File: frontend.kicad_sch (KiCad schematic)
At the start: 48 parts, among them J10 GND_CLIP, J3 RF-SHIELD-FRAME, J4 MOUNTING_HOLE, J5 MOUNTING_HOLE, J6 MOUNTING_HOLE, J7 MOUNTING_HOLE, P4 SMA, Q1 NMOS/PMOS, U12 MXD8638C, U13 TRF37C73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

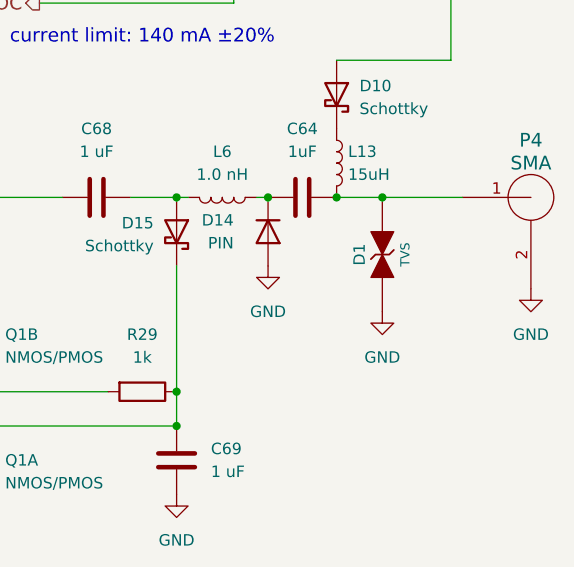
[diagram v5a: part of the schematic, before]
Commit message: Update TVS
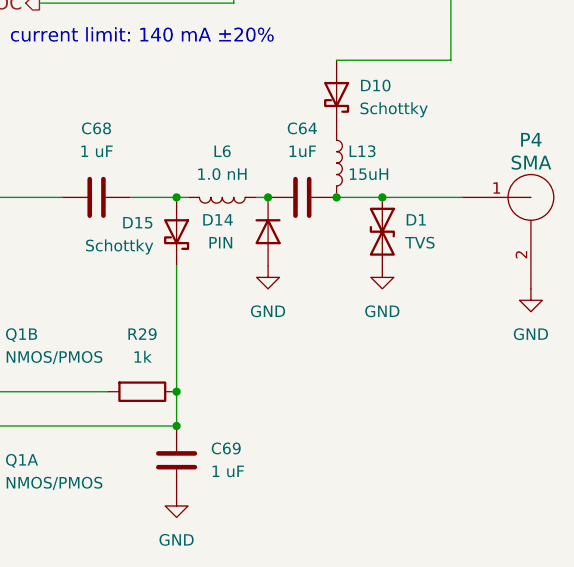
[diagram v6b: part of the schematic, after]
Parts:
- removed D1: TVS, hackrf:GSG-0402, symbol hackrf:GSG-DIODE-TVS-BI
- added D1: TVS, Diode_SMD:Nexperia_DSN0603-2_0.6x0.3mm_P0.4mm, symbol Device:D_TVS
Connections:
- net GND: now also D1.2 (A2)
- net at C64.2, L13.2, P4.1 (RF): now also D1.1 (A1)
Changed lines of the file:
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@@
 	)
 	(junction
-		(at 232.41 90.17)
-		(diameter 0)
-		(color 0 0 0 0)
-	)
-	(junction
 		(at 72.39 97.79)
 		(diameter 0)
@@
 	)
 	(junction
+		(at 232.41 90.17)
+		(diameter 0)
+		(color 0 0 0 0)
+	)
+	(junction
 		(at 127 62.23)
 		(diameter 0)
@@
 	(wire
 		(pts
+			(xy 232.41 90.17) (xy 241.3 90.17)
+		)
+		(stroke
+			(width 0)
+			(type default)
+		)
+	)
+	(wire
+		(pts
 			(xy 130.81 92.71) (xy 144.78 92.71)
 		)
@@
 	(wire
 		(pts
-			(xy 241.3 90.17) (xy 232.41 90.17)
+			(xy 227.33 90.17) (xy 232.41 90.17)
 		)
 		(stroke
@@
 	(wire
 		(pts
-			(xy 227.33 90.17) (xy 232.41 90.17)
-		)
-		(stroke
-			(width 0)
-			(type default)
-		)
-	)
-	(wire
-		(pts
 			(xy 165.1 119.38) (xy 165.1 92.71)
 		)
@@
 	)
 	(symbol
-		(lib_id "hackrf:GSG-DIODE-TVS-BI")
-		(at 232.41 96.52 90)
-		(unit 1)
-		(exclude_from_sim no)
-		(in_bom yes)
-		(on_board yes)
-		(dnp no)
-		(property "Reference" "D1"
-			(at 229.87 96.52 0)
-			(effects
-				(font
-					(size 1.27 1.27)
-				)
-			)
-		)
-		(property "Value" "TVS"
-			(at 234.95 96.52 0)
-			(effects
-				(font
-					(size 1.016 1.016)
-				)
-			)
-		)
-		(property "Footprint" "hackrf:GSG-0402"
-			(at 232.41 96.52 0)
-			(effects
-				(font
-					(size 1.524 1.524)
-				)
-				(hide yes)
-			)
-		)
-		(property "Datasheet" "~"
-			(at 232.41 96.52 0)
-			(effects
-				(font
-					(size 1.524 1.524)
-				)
-				(hide yes)
-			)
-		)
-		(property "Description" "TVS DIODE ESD .05PF 15KV 0402"
-			(at 232.41 96.52 0)
-			(effects
-				(font
-					(size 1.524 1.524)
-				)
-				(hide yes)
-			)
-		)
-		(property "Manufacturer" "TECH PUBLIC"
-			(at 232.41 96.52 0)
-			(effects
-				(font
-					(size 1.524 1.524)
-				)
-				(hide yes)
-			)
-		)
-		(property "Part Number" "LXES15AAA1-153"
-			(at 232.41 96.52 0)
-			(effects
-				(font
-					(size 1.524 1.524)
-				)
-				(hide yes)
-			)
-		)
-		(pin "1"
-		)
-		(pin "2"
-		)
-		(instances
-			(project ""
-				(path "/dba4afc6-760f-46cb-a936-032b76448f03/00000000-0000-0000-0000-0000503bb638"
-					(reference "D1")
-					(unit 1)
-				)
-			)
-		)
-	)
-	(symbol
 		(lib_id "Device:L")
 		(at 127 53.34 0)
@@
 	)
 	(symbol
+		(lib_id "Device:D_TVS")
+		(at 232.41 93.98 270)
+		(unit 1)
+		(exclude_from_sim no)
+		(in_bom yes)
+		(on_board yes)
+		(dnp no)
+		(fields_autoplaced yes)
+		(property "Reference" "D1"
+			(at 234.95 92.7099 90)
+			(effects
+				(font
+					(size 1.27 1.27)
+				)
+				(justify left)
+			)
+		)
+		(property "Value" "TVS"
+			(at 234.95 95.2499 90)
+			(effects
+				(font
+					(size 1.27 1.27)
+				)
+				(justify left)
+			)
+		)
+		(property "Footprint" "Diode_SMD:Nexperia_DSN0603-2_0.6x0.3mm_P0.4mm"
+			(at 232.41 93.98 0)
+			(effects
+				(font
+					(size 1.27 1.27)
+				)
+				(hide yes)
+			)
+		)
+		(property "Datasheet" "~"
+			(at 232.41 93.98 0)
+			(effects
+				(font
+					(size 1.27 1.27)
+				)
+				(hide yes)
+			)
+		)
+		(property "Description" "Bidirectional transient-voltage-suppression diode"
+			(at 232.41 93.98 0)
+			(effects
+				(font
+					(size 1.27 1.27)
+				)
+				(hide yes)
+			)
+		)
+		(property "Manufacturer" "Nexperia"
+			(at 232.41 93.98 0)
+			(effects
+				(font
+					(size 1.27 1.27)
+				)
+				(hide yes)
+			)
+		)
+		(property "Part Number" "PESD5V0H1BSFYL"
+			(at 232.41 93.98 0)
+			(effects
+				(font
+					(size 1.27 1.27)
+				)
+				(hide yes)
+			)
+		)
+		(property "Substitution" "PESD5V0H1BSF"
+			(at 232.41 93.98 0)
+			(effects
+				(font
+					(size 1.27 1.27)
+				)
+				(hide yes)
+			)
+		)
+		(pin "2"
+		)
+		(pin "1"
+		)
+		(instances
+			(project "praline"
+				(path "/dba4afc6-760f-46cb-a936-032b76448f03/00000000-0000-0000-0000-0000503bb638"
+					(reference "D1")
+					(unit 1)
+				)
+			)
+		)
+	)
+	(symbol
 		(lib_id "power:GND")
 		(at 152.4 48.26 0)
@@
 	(symbol
 		(lib_id "power:GND")
-		(at 232.41 102.87 0)
+		(at 232.41 97.79 0)
 		(unit 1)
 		(exclude_from_sim no)
@@
 		(fields_autoplaced yes)
 		(property "Reference" "#PWR057"
-			(at 232.41 109.22 0)
+			(at 232.41 104.14 0)
 			(effects
 				(font
@@
 		)
 		(property "Value" "GND"
-			(at 232.41 107.95 0)
+			(at 232.41 102.87 0)
 			(effects
 				(font
@@
 		)
 		(property "Footprint" ""
-			(at 232.41 102.87 0)
+			(at 232.41 97.79 0)
 			(effects
 				(font
@@
 		)
 		(property "Datasheet" ""
-			(at 232.41 102.87 0)
+			(at 232.41 97.79 0)
 			(effects
 				(font
@@
 		)
 		(property "Description" "Power symbol creates a global label with name \"GND\" , ground"
-			(at 232.41 102.87 0)
+			(at 232.41 97.79 0)
 			(effects
 				(font

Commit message: Update component selections
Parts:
- Q1: Part Number DMC2400UV -> DMC2400UV-7; Substitution (none) -> DMC2400UV*
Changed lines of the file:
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@@
 			)
 		)
-		(property "Part Number" "DMC2400UV"
+		(property "Part Number" "DMC2400UV-7"
+			(at 184.15 120.65 0)
+			(effects
+				(font
+					(size 1.27 1.27)
+				)
+				(hide yes)
+			)
+		)
+		(property "Substitution" "DMC2400UV*"
 			(at 184.15 120.65 0)
 			(effects
@@
 			)
 		)
-		(property "Part Number" "DMC2400UV"
+		(property "Part Number" "DMC2400UV-7"
 			(at 184.15 106.68 0)
 			(effects
+				(font
+					(size 1.27 1.27)
+				)
+				(hide yes)
+			)
+		)
+		(property "Substitution" "DMC2400UV*"
+			(at 184.15 106.68 0)
+			(effects

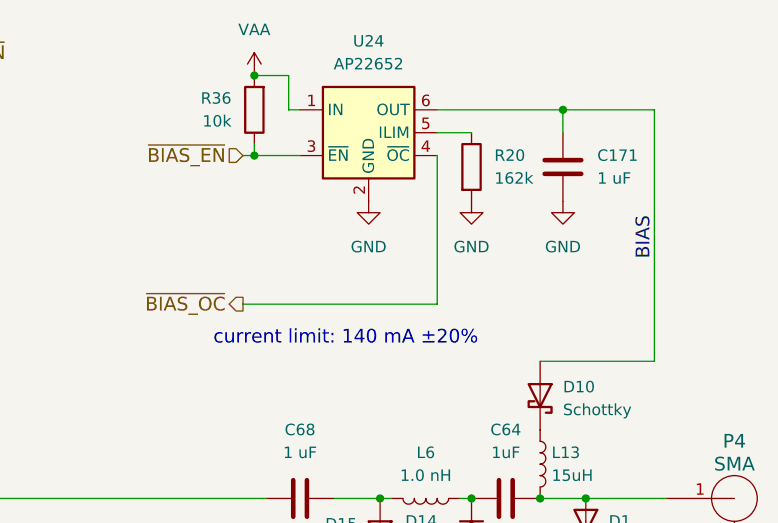
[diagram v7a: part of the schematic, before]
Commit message: Reduce antenna bias current limit to 125 mA
Change all 162k resistors to 180k
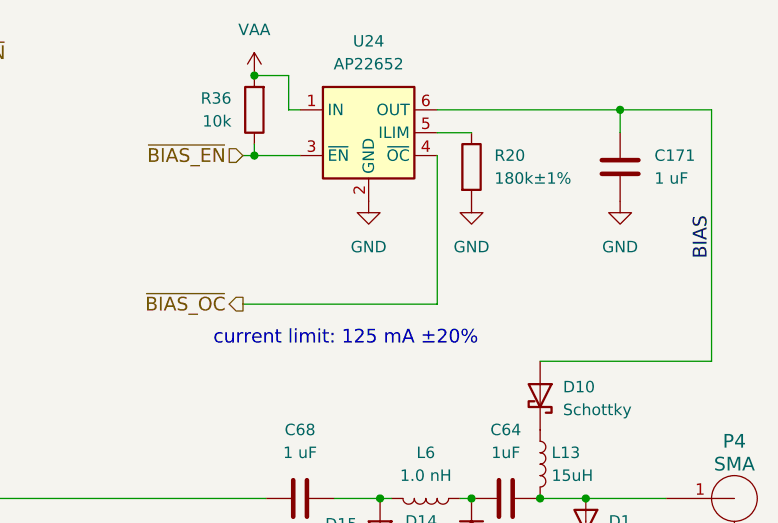
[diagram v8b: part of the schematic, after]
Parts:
- R20: value 162k -> 180k±1%; Part Number RC0402FR-07162KL -> RC0402FR-07180KL
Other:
- note added: "current limit: 125 mA ±20%"
- note removed: "current limit: 140 mA ±20%"
- moved on the sheet: C171
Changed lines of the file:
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@@
 	)
 	(junction
-		(at 229.87 46.99)
+		(at 236.22 46.99)
 		(diameter 0)
 		(color 0 0 0 0)
@@
 	(wire
 		(pts
-			(xy 227.33 74.93) (xy 240.03 74.93)
+			(xy 227.33 74.93) (xy 246.38 74.93)
 		)
 		(stroke
@@
 	(wire
 		(pts
-			(xy 229.87 46.99) (xy 229.87 49.53)
+			(xy 236.22 46.99) (xy 236.22 49.53)
 		)
 		(stroke
@@
 	(wire
 		(pts
-			(xy 240.03 74.93) (xy 240.03 46.99)
+			(xy 246.38 74.93) (xy 246.38 46.99)
 		)
 		(stroke
@@
 	(wire
 		(pts
-			(xy 240.03 46.99) (xy 229.87 46.99)
+			(xy 246.38 46.99) (xy 236.22 46.99)
 		)
 		(stroke
@@
 	(wire
 		(pts
-			(xy 215.9 46.99) (xy 229.87 46.99)
+			(xy 215.9 46.99) (xy 236.22 46.99)
 		)
 		(stroke
@@
 		)
 	)
-	(text "current limit: 140 mA ±20%"
+	(text "current limit: 125 mA ±20%"
 		(exclude_from_sim no)
 		(at 205.74 72.39 0)
@@
 	)
 	(label "BIAS"
-		(at 240.03 63.5 90)
+		(at 246.38 63.5 90)
 		(effects
 			(font
@@
 	(symbol
 		(lib_id "Device:C")
-		(at 229.87 53.34 0)
+		(at 236.22 53.34 0)
 		(unit 1)
 		(exclude_from_sim no)
@@
 		(fields_autoplaced yes)
 		(property "Reference" "C171"
-			(at 233.68 52.0699 0)
+			(at 240.03 52.0699 0)
 			(effects
 				(font
@@
 		)
 		(property "Value" "1 uF"
-			(at 233.68 54.6099 0)
+			(at 240.03 54.6099 0)
 			(effects
 				(font
@@
 		)
 		(property "Footprint" "Capacitor_SMD:C_0201_0603Metric"
-			(at 229.87 53.34 0)
+			(at 236.22 53.34 0)
 			(effects
 				(font
@@
 		)
 		(property "Datasheet" "~"
-			(at 229.87 53.34 0)
+			(at 236.22 53.34 0)
 			(effects
 				(font
@@
 		)
 		(property "Description" "CAP CER 1UF 10V X5R 0201"
-			(at 229.87 53.34 0)
+			(at 236.22 53.34 0)
 			(effects
 				(font
@@
 		)
 		(property "Manufacturer" "Murata"
-			(at 229.87 53.34 0)
+			(at 236.22 53.34 0)
 			(effects
 				(font
@@
 		)
 		(property "Part Number" "GRM033R61A105ME44D"
-			(at 229.87 53.34 0)
+			(at 236.22 53.34 0)
 			(effects
 				(font
@@
 		)
 		(property "Substitution" "GRM033R61A105ME44*, GRM033R61C105ME15*, Samsung CL03A105MO3NRN*"
-			(at 229.87 53.34 0)
+			(at 236.22 53.34 0)
 			(effects
 				(font
@@
 			)
 		)
-		(property "Value" "162k"
+		(property "Value" "180k±1%"
 			(at 222.25 54.6099 0)
 			(effects
@@
 			)
 		)
-		(property "Description" "RES 1/16W 162K OHM 1% 0402"
+		(property "Description" "RES 180K OHM 1% 1/16W 0402"
 			(at 219.71 53.34 0)
 			(effects
@@
 			)
 		)
-		(property "Part Number" "RC0402FR-07162KL"
+		(property "Part Number" "RC0402FR-07180KL"
 			(at 219.71 53.34 0)
 			(effects
@@
 	(symbol
 		(lib_id "power:GND")
-		(at 229.87 57.15 0)
+		(at 236.22 57.15 0)
 		(unit 1)
 		(exclude_from_sim no)
@@
 		(fields_autoplaced yes)
 		(property "Reference" "#PWR0108"
-			(at 229.87 63.5 0)
+			(at 236.22 63.5 0)
 			(effects
 				(font
@@
 		)
 		(property "Value" "GND"
-			(at 229.87 62.23 0)
+			(at 236.22 62.23 0)
 			(effects
 				(font
@@
 		)
 		(property "Footprint" ""
-			(at 229.87 57.15 0)
+			(at 236.22 57.15 0)
 			(effects
 				(font
@@
 		)
 		(property "Datasheet" ""
-			(at 229.87 57.15 0)
+			(at 236.22 57.15 0)
 			(effects
 				(font
@@
 		)
 		(property "Description" "Power symbol creates a global label with name \"GND\" , ground"
-			(at 229.87 57.15 0)
+			(at 236.22 57.15 0)
 			(effects
 				(font
